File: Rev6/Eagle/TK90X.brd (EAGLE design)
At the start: 217.8 x 132.1 mm, 222 parts, among them IC1 Z80, IC10 74LS365N, IC11 LM1886, IC12 LM1889, IC13 4116, IC14 4116, IC15 4116, IC16 4116, IC17 4116, IC18 4116, IC19 4116, IC2 ROM, IC20 4116, IC21 4416, IC22 4416, IC23 4416, IC24 4416, IC25 74LS00, IC26 74LS00, IC27 74LS32, IC28 74LS04, IC3 ULA TK90, IC4 74LS74, IC5 74LS74, IC6 74LS157, IC7 74LS157, IC8 74LS157, IC9 74LS157, J1 0R-JUMPB, J2 0R-JUMPB, Q1 BC548, Q2 BC548, Q3 BF494, Q4 BC548, Q5 BD139, Q6 BD136, Q7 BC548, Q8 BC517, X1 RCA2PINA1, X2 POWER

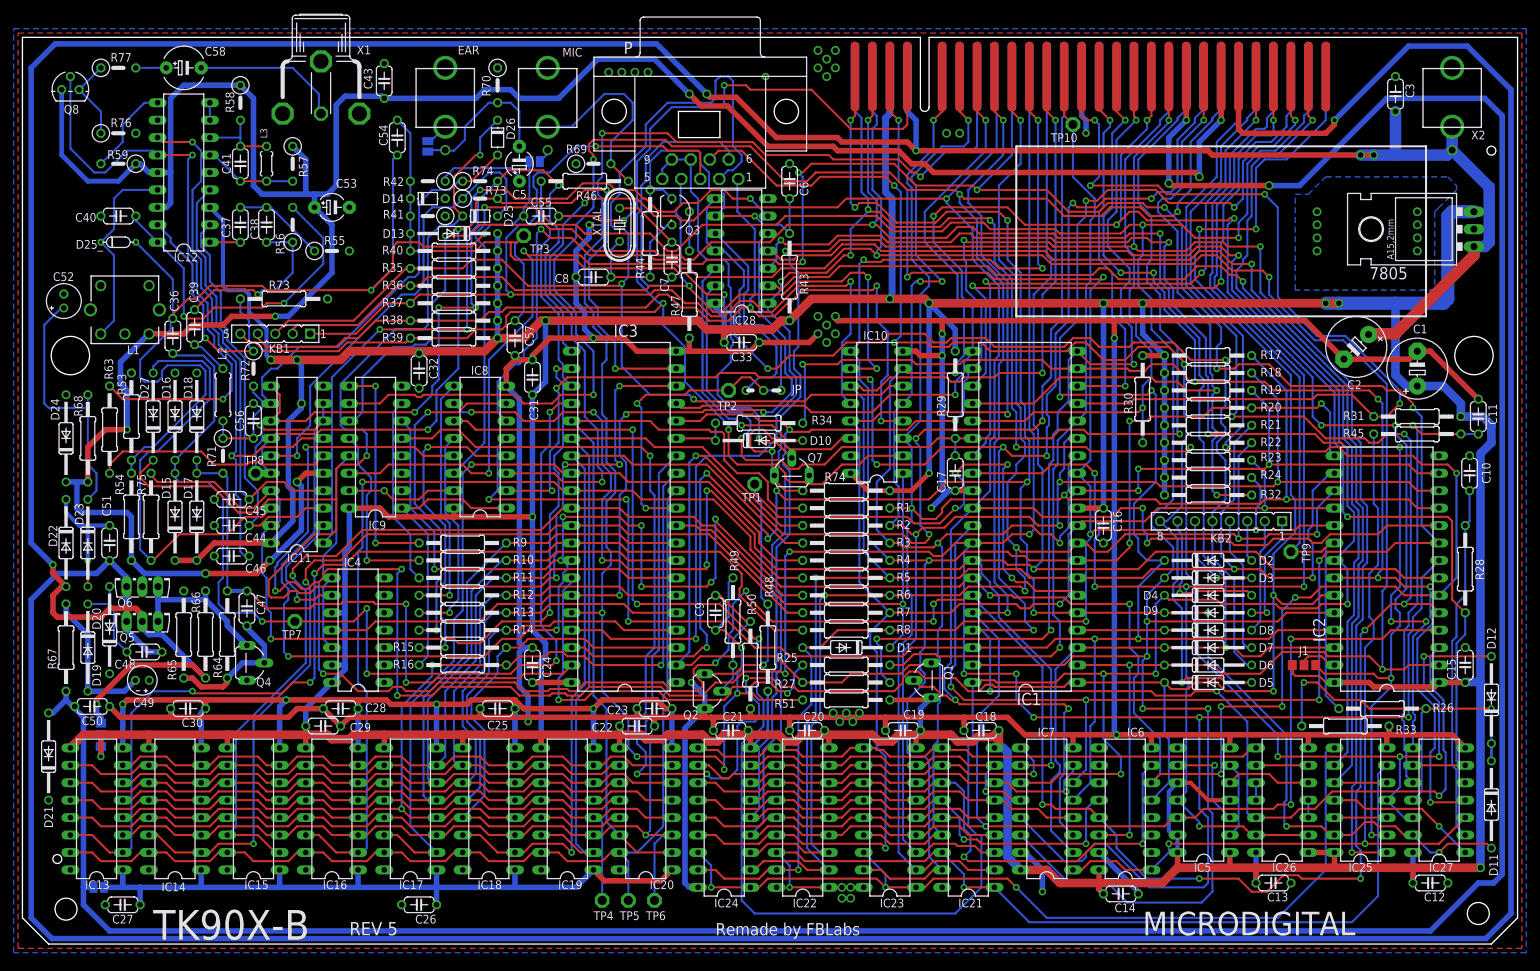
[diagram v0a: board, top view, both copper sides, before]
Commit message: Corrigido conexões power Adicionado jumpers de solda pros jacks de áudio Adicionado revisão 6 com 74LS365 substituido pelo 74LS244
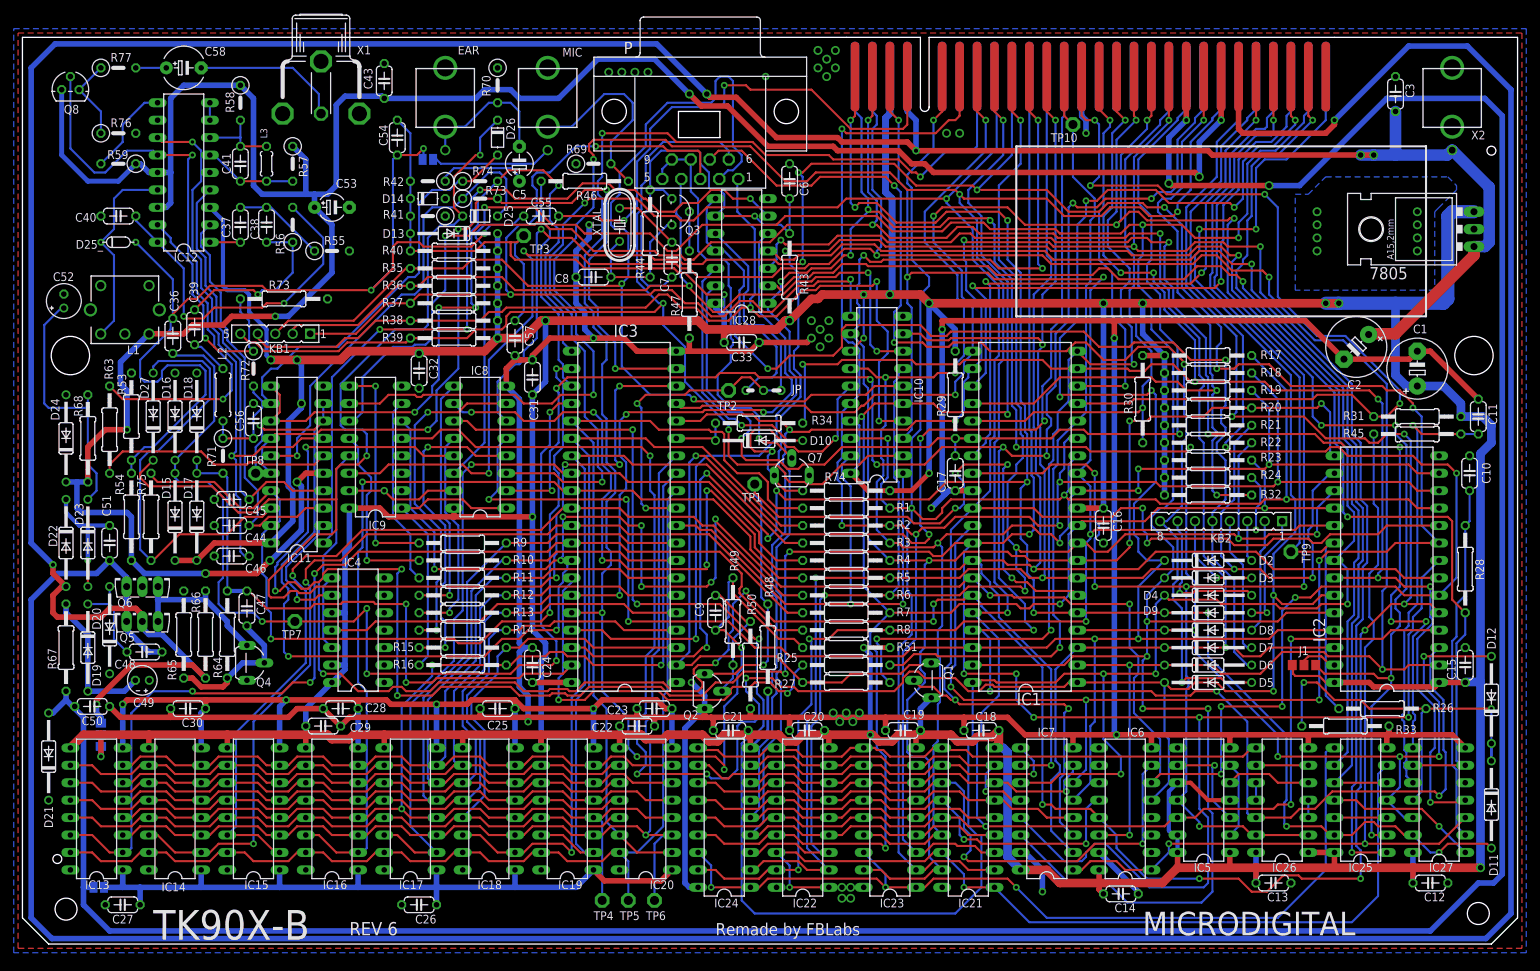
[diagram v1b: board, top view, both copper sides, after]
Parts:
- removed D1: 1N4148, tk90:DO35-12
- removed J5: (no value), jumper:SJ
- IC10: value 74LS365N -> 74LS244N; device tk90:DIL16 -> tk90:DIL20
- moved J4 15.6 mm to (59.1, 114.3)
- moved R51 7.62 mm to (120.0, 43.2)
- moved IC10 2.54 mm to (124.5, 80.0)
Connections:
- removed net N$88: EAR.NC, J5.2
- net !KBD: now also IC10.19; no longer D1.C
- net +5V: now also IC10.13, IC10.17, IC10.20; no longer IC10.16
- net D0: now also IC10.18; no longer IC10.3
- net D1: now also IC10.16; no longer IC10.5
- net D2: now also IC10.14; no longer IC10.7
- net D3: now also IC10.12; no longer IC10.9
- net D4: now also IC10.9; no longer IC10.11
- net D5: now also IC10.7
- net D6: now also IC10.5; no longer IC10.13
- net D7: now also IC10.3; no longer D1.A
- net GND: now also IC10.10; no longer IC10.15, IC10.8
- net N$16: now also EAR.NC; no longer J5.1
- net N$27: now also IC10.8; no longer IC10.10
- net N$28: now also IC10.11; no longer IC10.12
- net N$29: now also IC10.15; no longer IC10.14
- net V+: no longer X2.NC
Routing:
- net D5: track 231.9 -> 265.9 mm
- net +5V: track 1026.8 -> 1055.5 mm, vias 14 -> 18
- net D7: track 249.1 -> 272.8 mm, vias 7 -> 8
- net GND: track 627.2 -> 604.0 mm, vias 48 -> 47
- net N$50: track 2.14 -> 17.8 mm
- net !KBD: track 63.9 -> 79.4 mm, vias 1 -> 2
- net D0: track 249.3 -> 264.7 mm, vias 4 -> 5
- net N$28: track 155.7 -> 142.6 mm
- net D1: track 254.8 -> 267.7 mm, vias 7 -> 6
- net D4: track 277.0 -> 269.0 mm, vias 5 -> 6
- net N$29: track 31.7 -> 38.2 mm, vias 1 -> 2
- net D2: track 247.1 -> 253.2 mm, vias 7 -> 8
- net CLK: track 228.0 -> 233.8 mm, vias 7 -> 6
- net V+: track 411.4 -> 408.0 mm
- net N$88: track 3.41 -> 0.00 mm
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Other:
- board text added: "REV 6"
- board text removed: "REV 5"

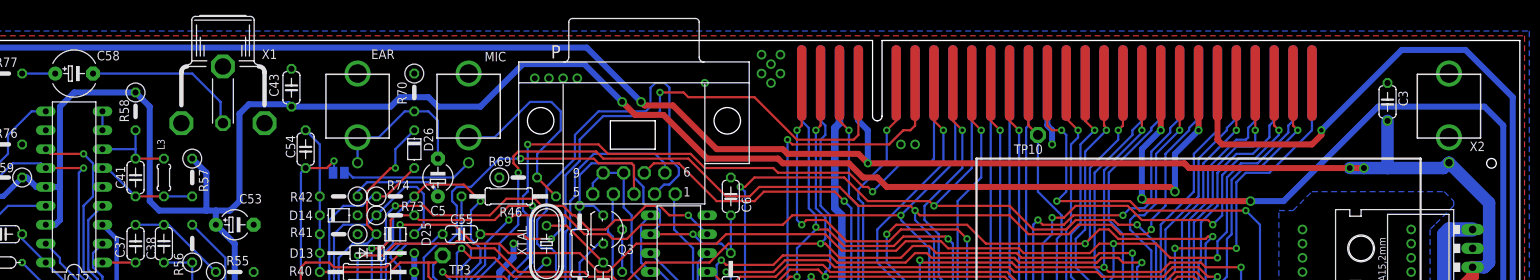
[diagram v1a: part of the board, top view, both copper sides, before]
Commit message: Corrigido valor de R49 e outros pequenos detalhes
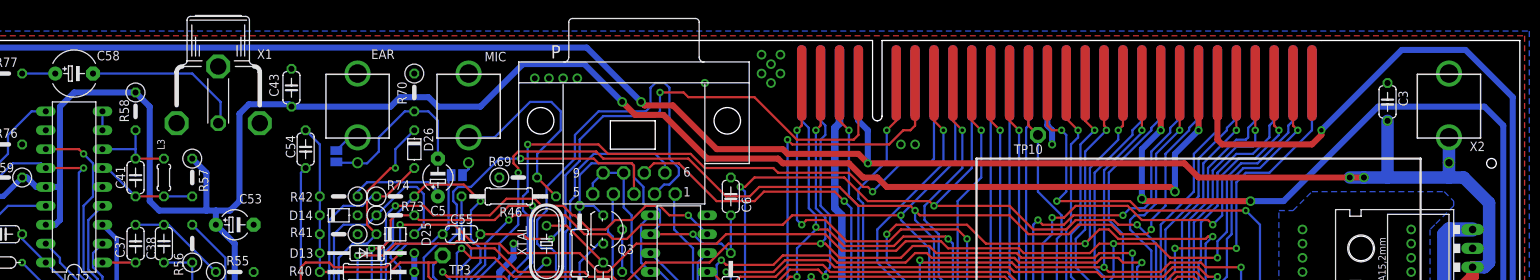
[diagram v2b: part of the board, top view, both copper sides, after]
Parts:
- added J5: (no value), jumper:SJ
- R49: value 1K -> 4K7
- moved J4 15.9 mm to (74.9, 114.0)
- moved X1 0.64 mm to (42.9, 123.5)
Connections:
- new net N$88: EAR.NC, J5.2
- net N$16: now also J5.1; no longer EAR.NC
- net V+: now also X2.NC
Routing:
- net N$50: track 17.8 -> 2.01 mm
- net V+: track 408.0 -> 414.0 mm
- net N$88: track 0.00 -> 3.60 mm
- net AUDIO: track 143.6 -> 146.1 mm, vias 3 -> 2
- net N$16: track 21.3 -> 23.3 mm

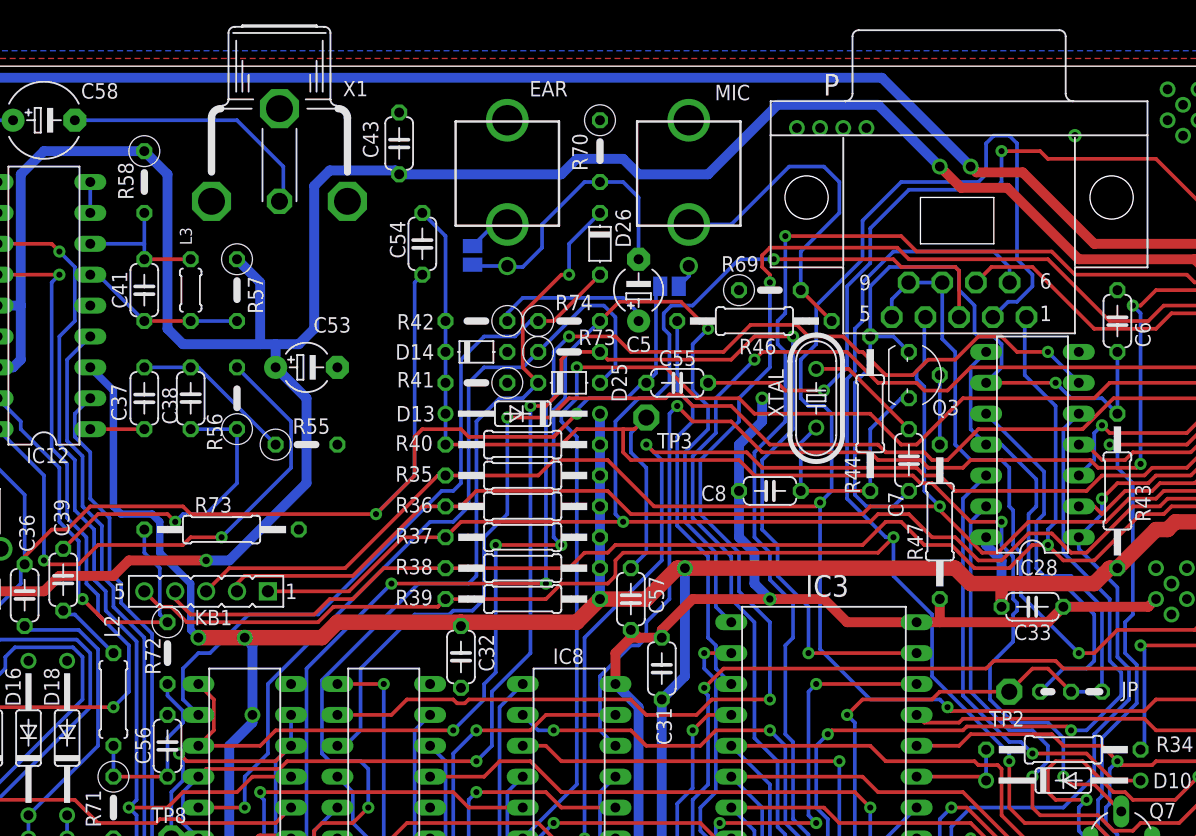
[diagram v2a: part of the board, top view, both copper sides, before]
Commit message: Corrigindo footprint dos jacks RCA Corrigindo lista de peças da revisão 7
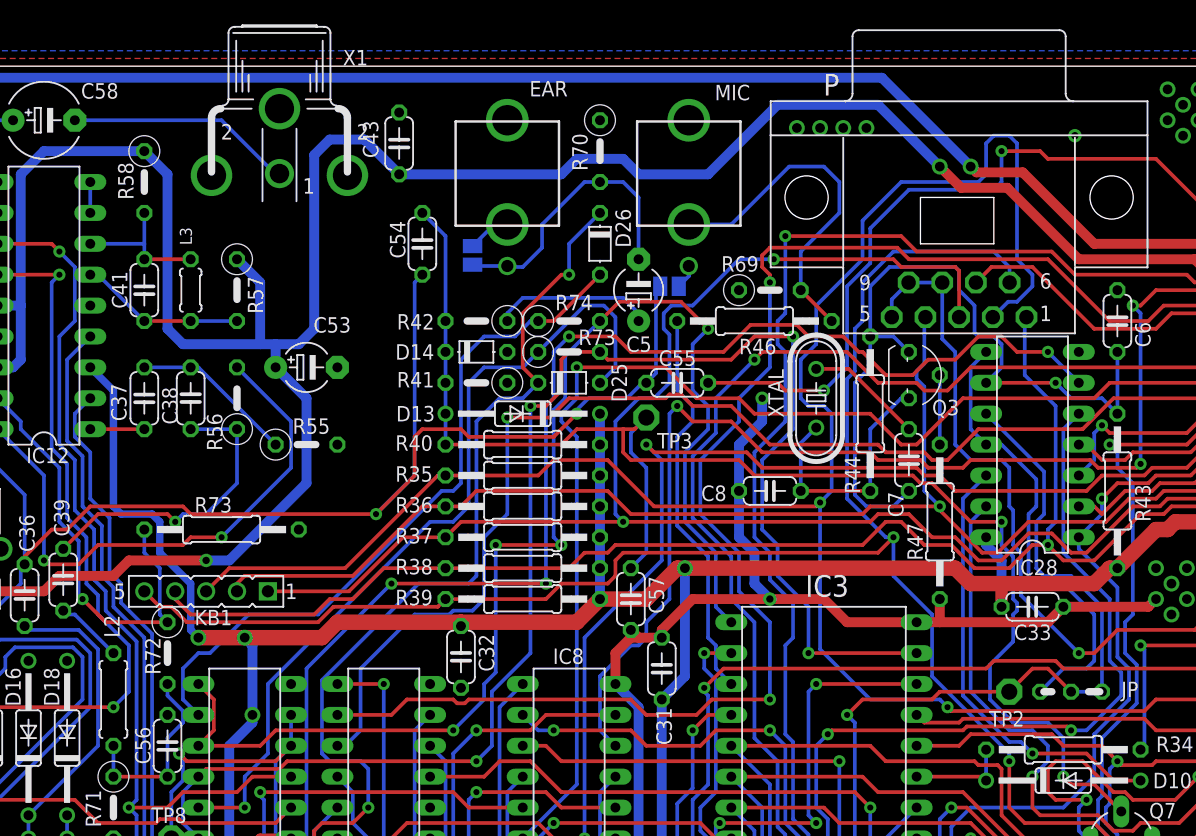
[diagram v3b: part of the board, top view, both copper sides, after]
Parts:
- X1: value RCA2PINA1 -> RCA2PINN1; device tk90:TOBU3 -> tk90:DX1
- moved X1 2.54 mm to (42.9, 126.0)
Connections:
- net !ROMCS: now also TP9.TP; no longer TP9.1
- net !VCAS: now also TP5.TP; no longer TP5.1
- net !VRAS: now also TP4.TP; no longer TP4.1
- net !VWR: now also TP6.TP; no longer TP6.1
- net /INT: now also TP10.TP; no longer TP10.1
- net BEEP: now also TP7.TP; no longer TP7.1
- net GND: now also X1.2, X1.2@1, X1.2@2; no longer X1.SHELL, X1.SHELL@1, X1.SHELL@2
- net N$47: now also TP2.TP; no longer TP2.1
- net N$54: now also TP8.TP; no longer TP8.1
- net N$74: now also X1.1; no longer X1.PIN
- net SNDIN: now also TP3.TP; no longer TP3.1
- net Z80CLK: now also TP1.TP; no longer TP1.1
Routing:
- net +12V: track 390.1 -> 393.7 mm
- net N$74: track 21.7 -> 18.6 mm
